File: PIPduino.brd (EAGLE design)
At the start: 46 x 46 mm, 41 parts, among them IC1 ATmega328P\, IC2 SPX1117, J1 ISP/SPI

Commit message: Added 5th I2C, fixed silk for VIN
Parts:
- removed JP2: 5V, pinhead-2:1X04-S
- removed JP3: SDA, pinhead-2:1X04-S
- removed JP4: SCL, pinhead-2:1X04-S
- removed JP5: GND, pinhead-2:1X04-S
- added JP23: SCL, pinhead-2:1X05-S
- added JP24: GND, pinhead-2:1X05-S
- added JP25: 5V, pinhead-2:1X05-S
- added JP26: SDA, pinhead-2:1X05-S
- moved R1 1.93 mm to (41.8, 10.3)
- moved R2 1.70 mm to (43.3, 10.3)
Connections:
- net 5V: now also JP25.1, JP25.2, JP25.3, JP25.4, JP25.5; no longer JP2.1, JP2.2, JP2.3, JP2.4
- net GND: now also JP24.1, JP24.2, JP24.3, JP24.4, JP24.5; no longer JP5.1, JP5.2, JP5.3, JP5.4
- net SCL: now also JP23.1, JP23.2, JP23.3, JP23.4, JP23.5; no longer JP4.1, JP4.2, JP4.3, JP4.4
- net SDA: now also JP26.1, JP26.2, JP26.3, JP26.4, JP26.5; no longer JP3.1, JP3.2, JP3.3, JP3.4
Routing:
- net SDA: track 31.7 -> 33.8 mm
- net SCL: track 34.5 -> 35.6 mm
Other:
- board text added: "6.1-15V"
- board text added: "Rev 0.2"
- board text removed: "5.5-26V"
- board text removed: "Rev 0.1"

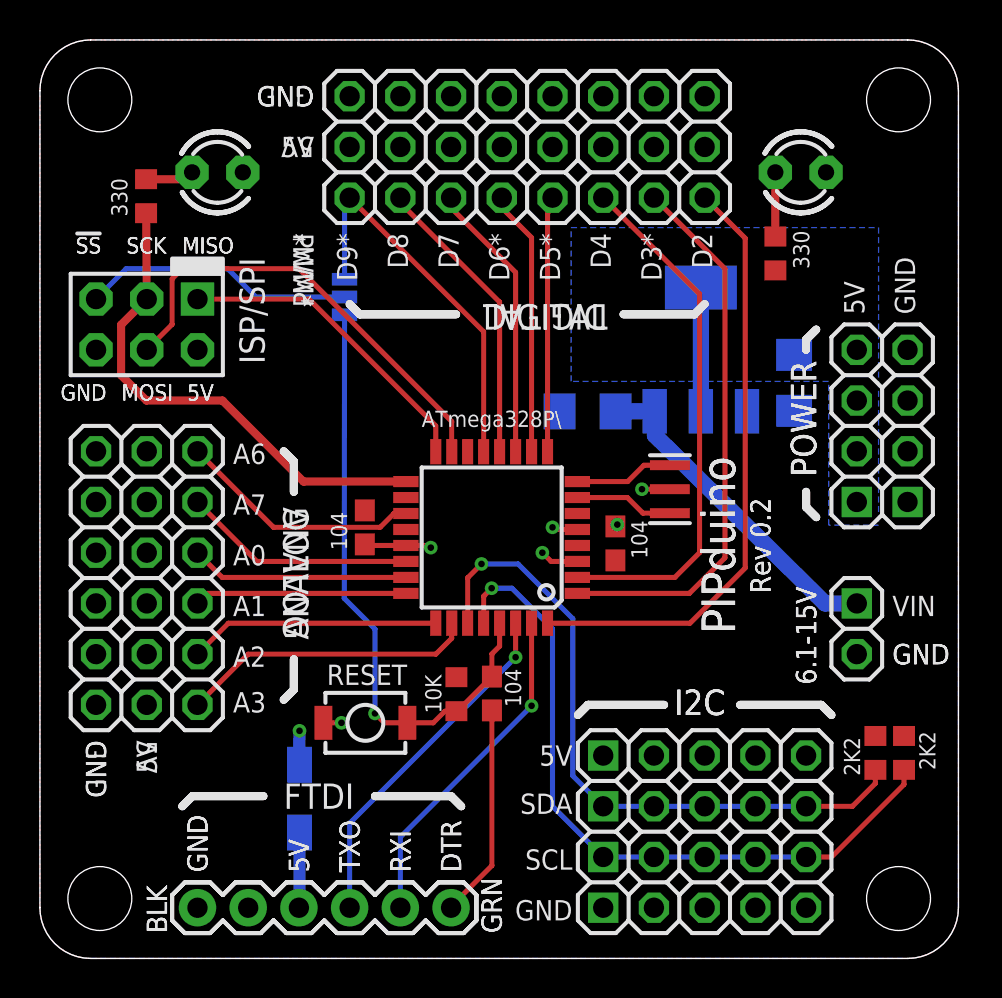
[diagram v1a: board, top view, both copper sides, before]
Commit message: Revised power pin silk to be more visible; moved rev silk to make room.
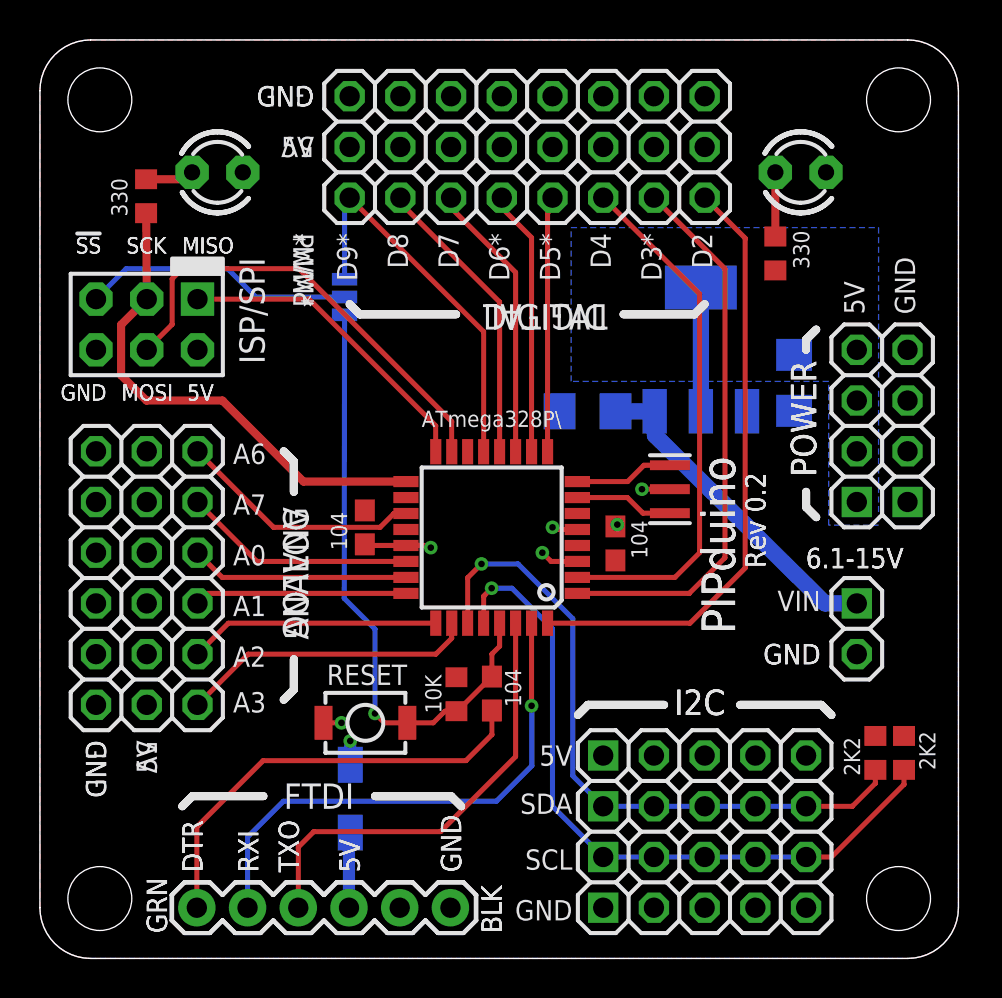
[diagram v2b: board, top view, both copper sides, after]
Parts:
- moved JP1 12.7 mm to (7.86, 2.54), turned to 0 degrees
- moved D1 2.54 mm to (15.5, 8.00)
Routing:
- net N$15: track 10.7 -> 22.0 mm
- net RXI: track 17.0 -> 26.4 mm
- net TXO: track 17.7 -> 22.5 mm, vias 1 -> 0
